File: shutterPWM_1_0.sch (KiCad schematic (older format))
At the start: 33 parts, among them P11 Header_R/A_2x3, P12 Header_R/A_2x3, U2 DRV103, U3 DRV103, U4 MCP4728

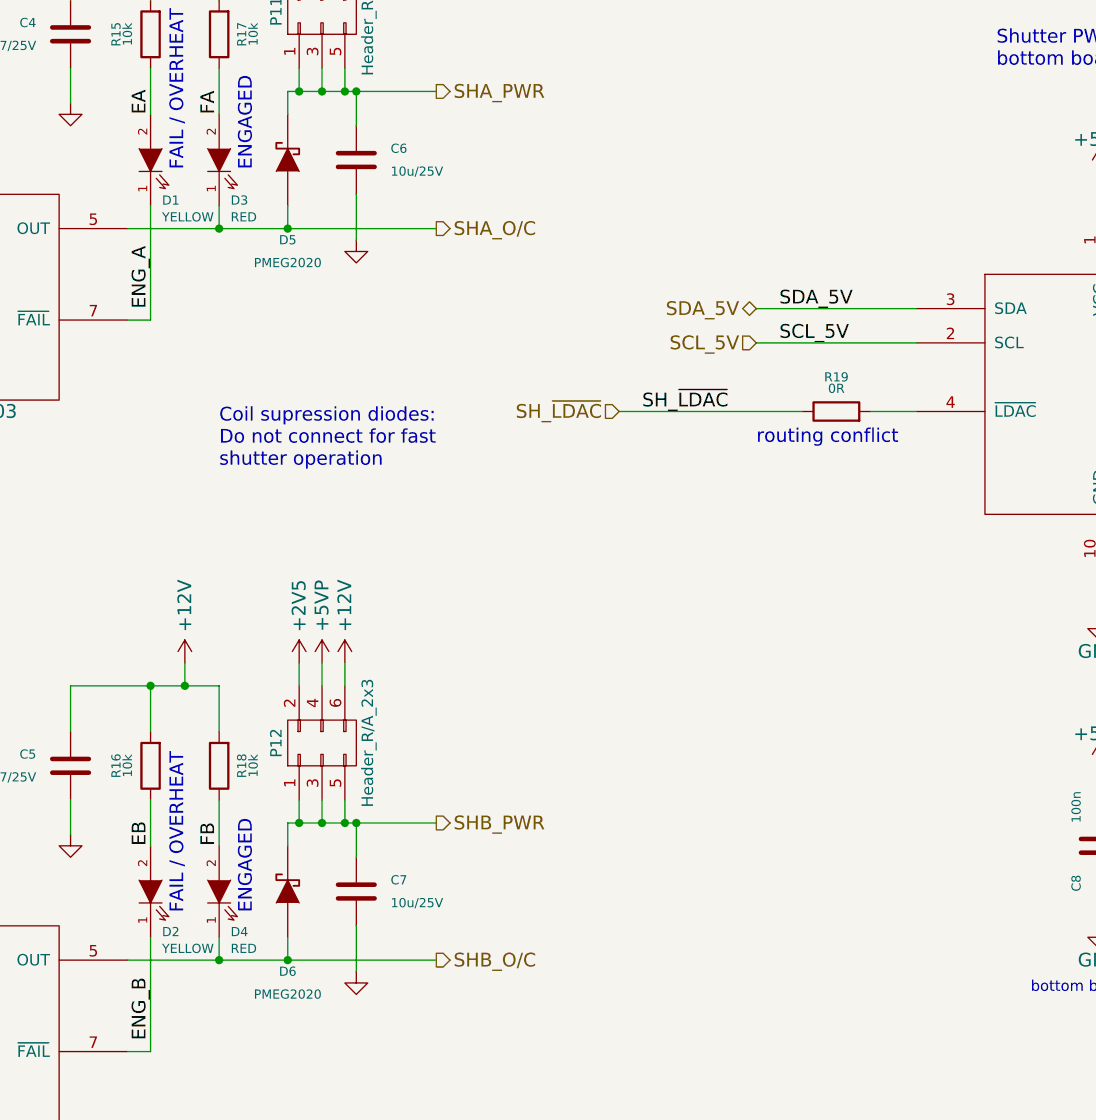
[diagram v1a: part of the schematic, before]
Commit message: Added component descriptions
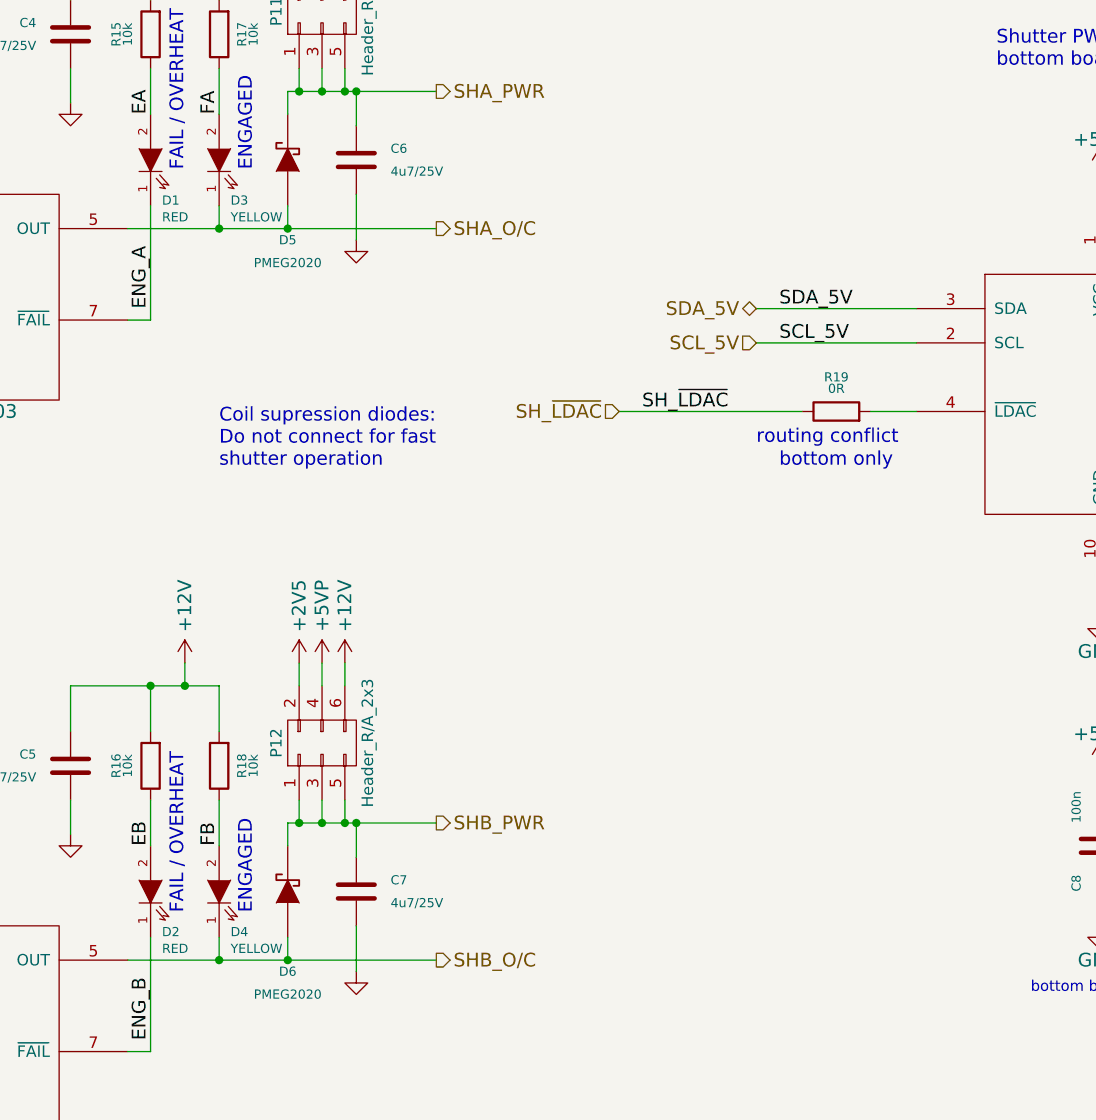
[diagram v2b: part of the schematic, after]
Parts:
- C2, C3: Order Code 9306352 -> 9406352; Supplier (none) -> Farnell
- C6, C7: value 10u/25V -> 4u7/25V; Order Code 2426961 -> 2362111; Part Number GRM219R61E106KA12D -> GRM21BR61E475MA12L
- D1, D2: value YELLOW -> RED
- D3, D4: value RED -> YELLOW; Manufacturer Osram -> Avago; Order Code 1226417 -> 8554773; Part Number LYN971-Z -> HSMY-C150
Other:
- note added: "bottom only"
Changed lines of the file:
@@
 F 4 "MCU0805R103KCT" V 2800 2800 60  0001 C CNN "Part Number"
 F 5 "Multicomp" V 2800 2800 60  0001 C CNN "Manufacturer"
-F 6 "9306352" V 2800 2800 60  0001 C CNN "Order Code"
+F 6 "Farnell" H 2800 2800 60  0001 C CNN "Supplier"
+F 7 "9406352" V 2800 2800 60  0001 C CNN "Order Code"
 	1    2800 2800
 	0    -1   -1   0
@@
 AR Path="/54E08E01/55463929" Ref="C6"  Part="1"
 F 0 "C6" H 5400 2250 40  0000 R CNN
-F 1 "10u/25V" H 5400 2350 40  0000 R CNN
+F 1 "4u7/25V" H 5400 2350 40  0000 R CNN
 F 2 "Capacitors_SMD:C_0805" H 5588 2150 30  0001 C CNN
 F 3 "" H 5550 2300 60  0000 C CNN
-F 4 "GRM219R61E106KA12D" H 5550 2300 60  0001 C CNN "Part Number"
+F 4 "GRM21BR61E475MA12L" H 5550 2300 60  0001 C CNN "Part Number"
 F 5 "Murata" H 5550 2300 60  0001 C CNN "Manufacturer"
-F 6 "2426961" H 5550 2300 60  0001 C CNN "Order Code"
+F 6 "2362111" H 5550 2300 60  0001 C CNN "Order Code"
 	1    5550 2300
 	-1   0    0    1
@@
 AR Path="/54E08E01/5567D38B" Ref="D1"  Part="1"
 F 0 "D1" V 4450 2250 40  0000 R TNN
-F 1 "YELLOW" V 4400 2250 40  0000 R CNN
+F 1 "RED" V 4400 2250 40  0000 R CNN
 F 2 "LEDs:LED-1206" H 4650 2300 60  0001 C CNN
 F 3 "" H 4650 2300 60  0000 C CNN
@@
 AR Path="/54E08E01/556888A1" Ref="D3"  Part="1"
 F 0 "D3" V 4750 2250 40  0000 R TNN
-F 1 "RED" V 4700 2250 40  0000 R CNN
+F 1 "YELLOW" V 4700 2250 40  0000 R CNN
 F 2 "LEDs:LED-1206" H 4950 2300 60  0001 C CNN
 F 3 "" H 4950 2300 60  0000 C CNN
-F 4 "LYN971-Z" H 4950 2300 60  0001 C CNN "Part Number"
-F 5 "Osram" V 4950 2300 60  0001 C CNN "Manufacturer"
-F 6 "1226417" H 4950 2300 60  0001 C CNN "Order Code"
+F 4 "HSMY-C150" H 4950 2300 60  0001 C CNN "Part Number"
+F 5 "Avago" V 4950 2300 60  0001 C CNN "Manufacturer"
+F 6 "8554773" H 4950 2300 60  0001 C CNN "Order Code"
 	1    4950 2300
 	0    -1   -1   0
@@
 AR Path="/54E08E01/55C117E9" Ref="C7"  Part="1"
 F 0 "C7" H 5400 5450 40  0000 R CNN
-F 1 "10u/25V" H 5400 5550 40  0000 R CNN
+F 1 "4u7/25V" H 5400 5550 40  0000 R CNN
 F 2 "Capacitors_SMD:C_0805" H 5588 5350 30  0001 C CNN
 F 3 "" H 5550 5500 60  0000 C CNN
-F 4 "GRM219R61E106KA12D" H 5550 5500 60  0001 C CNN "Part Number"
+F 4 "GRM21BR61E475MA12L" H 5550 5500 60  0001 C CNN "Part Number"
 F 5 "Murata" H 5550 5500 60  0001 C CNN "Manufacturer"
-F 6 "2426961" H 5550 5500 60  0001 C CNN "Order Code"
+F 6 "2362111" H 5550 5500 60  0001 C CNN "Order Code"
 	1    5550 5500
 	-1   0    0    1
@@
 F 4 "MCU0805R103KCT" V 2800 6000 60  0001 C CNN "Part Number"
 F 5 "Multicomp" V 2800 6000 60  0001 C CNN "Manufacturer"
-F 6 "9306352" V 2800 6000 60  0001 C CNN "Order Code"
+F 6 "Farnell" H 2800 6000 60  0001 C CNN "Supplier"
+F 7 "9406352" V 2800 6000 60  0001 C CNN "Order Code"
 	1    2800 6000
 	0    -1   -1   0
@@
 P 4650 5500
 F 0 "D2" V 4450 5450 40  0000 R TNN
-F 1 "YELLOW" V 4400 5450 40  0000 R CNN
+F 1 "RED" V 4400 5450 40  0000 R CNN
 F 2 "LEDs:LED-1206" H 4650 5500 60  0001 C CNN
 F 3 "" H 4650 5500 60  0000 C CNN
@@
 P 4950 5500
 F 0 "D4" V 4750 5450 40  0000 R TNN
-F 1 "RED" V 4700 5450 40  0000 R CNN
+F 1 "YELLOW" V 4700 5450 40  0000 R CNN
 F 2 "LEDs:LED-1206" H 4950 5500 60  0001 C CNN
 F 3 "" H 4950 5500 60  0000 C CNN
-F 4 "LYN971-Z" H 4950 5500 60  0001 C CNN "Part Number"
-F 5 "Osram" V 4950 5500 60  0001 C CNN "Manufacturer"
-F 6 "1226417" H 4950 5500 60  0001 C CNN "Order Code"
+F 4 "HSMY-C150" H 4950 5500 60  0001 C CNN "Part Number"
+F 5 "Avago" V 4950 5500 60  0001 C CNN "Manufacturer"
+F 6 "8554773" H 4950 5500 60  0001 C CNN "Order Code"
 	1    4950 5500
 	0    -1   -1   0
 $EndComp
+Text Notes 7400 3650 0    60   ~ 0
+bottom only
 $EndSCHEMATC
